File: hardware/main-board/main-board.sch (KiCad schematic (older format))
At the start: 76 parts, among them J1 USB_B_Micro, J2 STDC14, J3 Display Connector, J4 Conn_01x02, SW1 SW_Push, SW2 SW_Push, SW3 SW_Push, SW4 SW_Push, SW5 SW_Detect, U1 TSL2591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

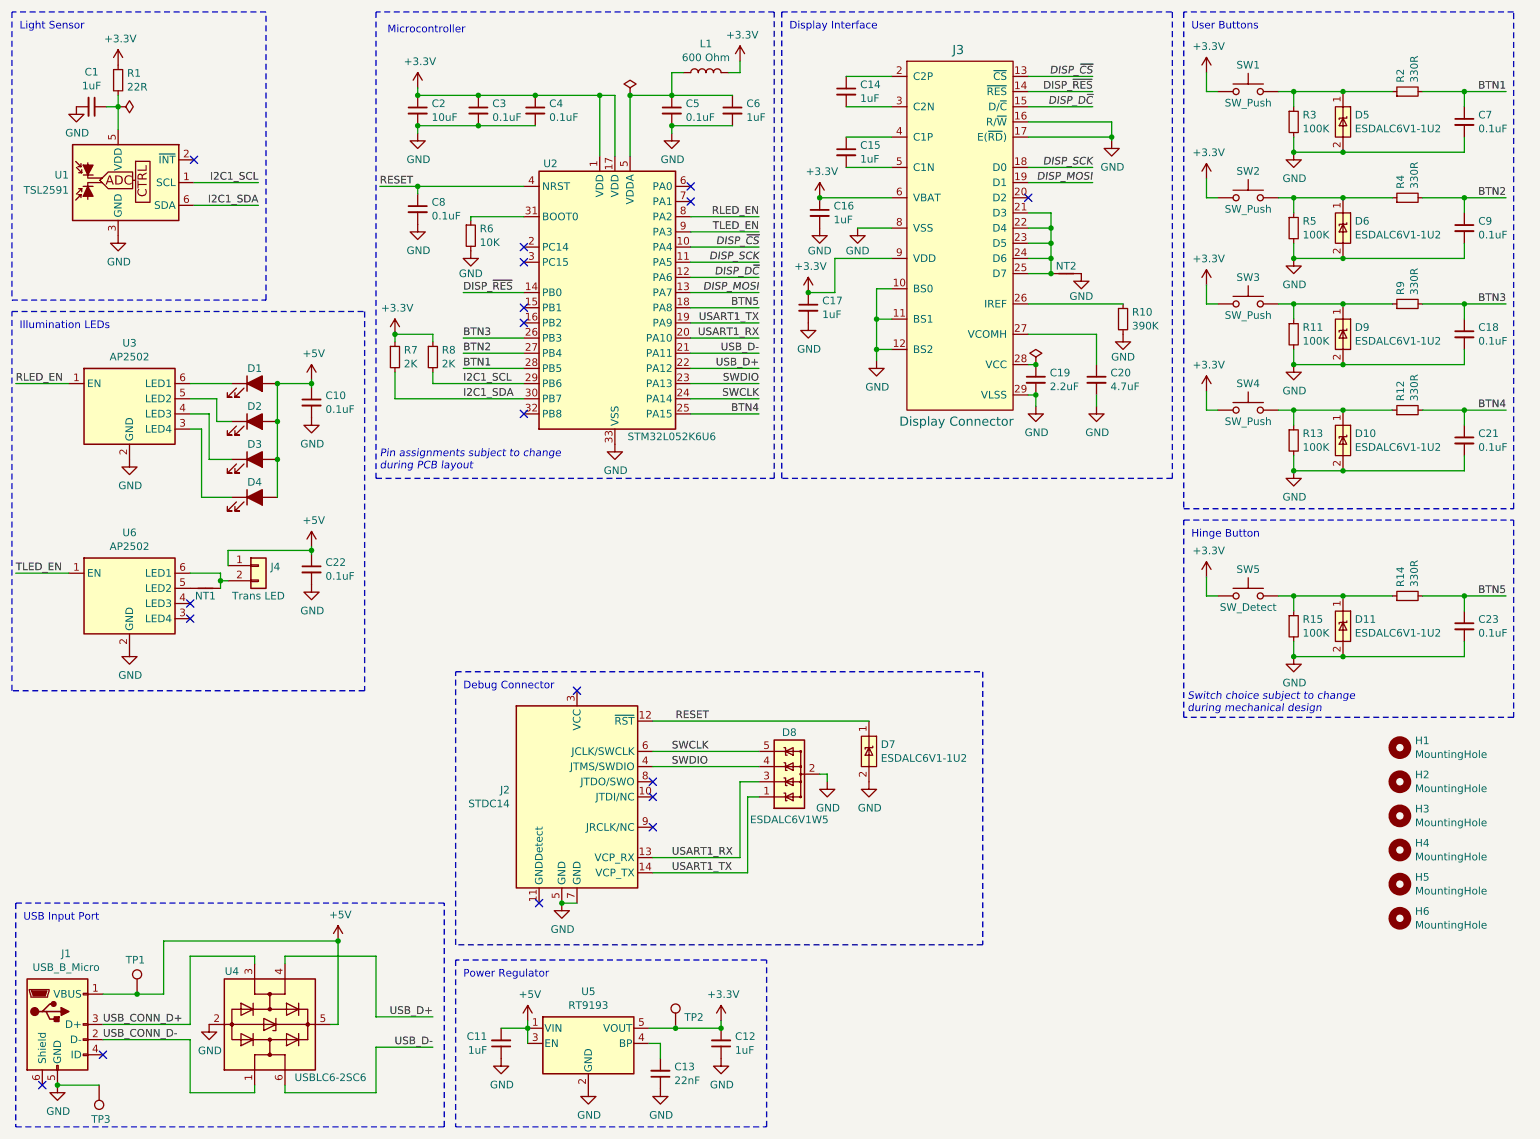
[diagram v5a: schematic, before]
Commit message: Power filtering changes
Added polyfuse and ferrite bead to Vbus power input.
Changed ferrite bead on VDDA to match the one used on the power input,
since they have similar specs and the other one was EOL.
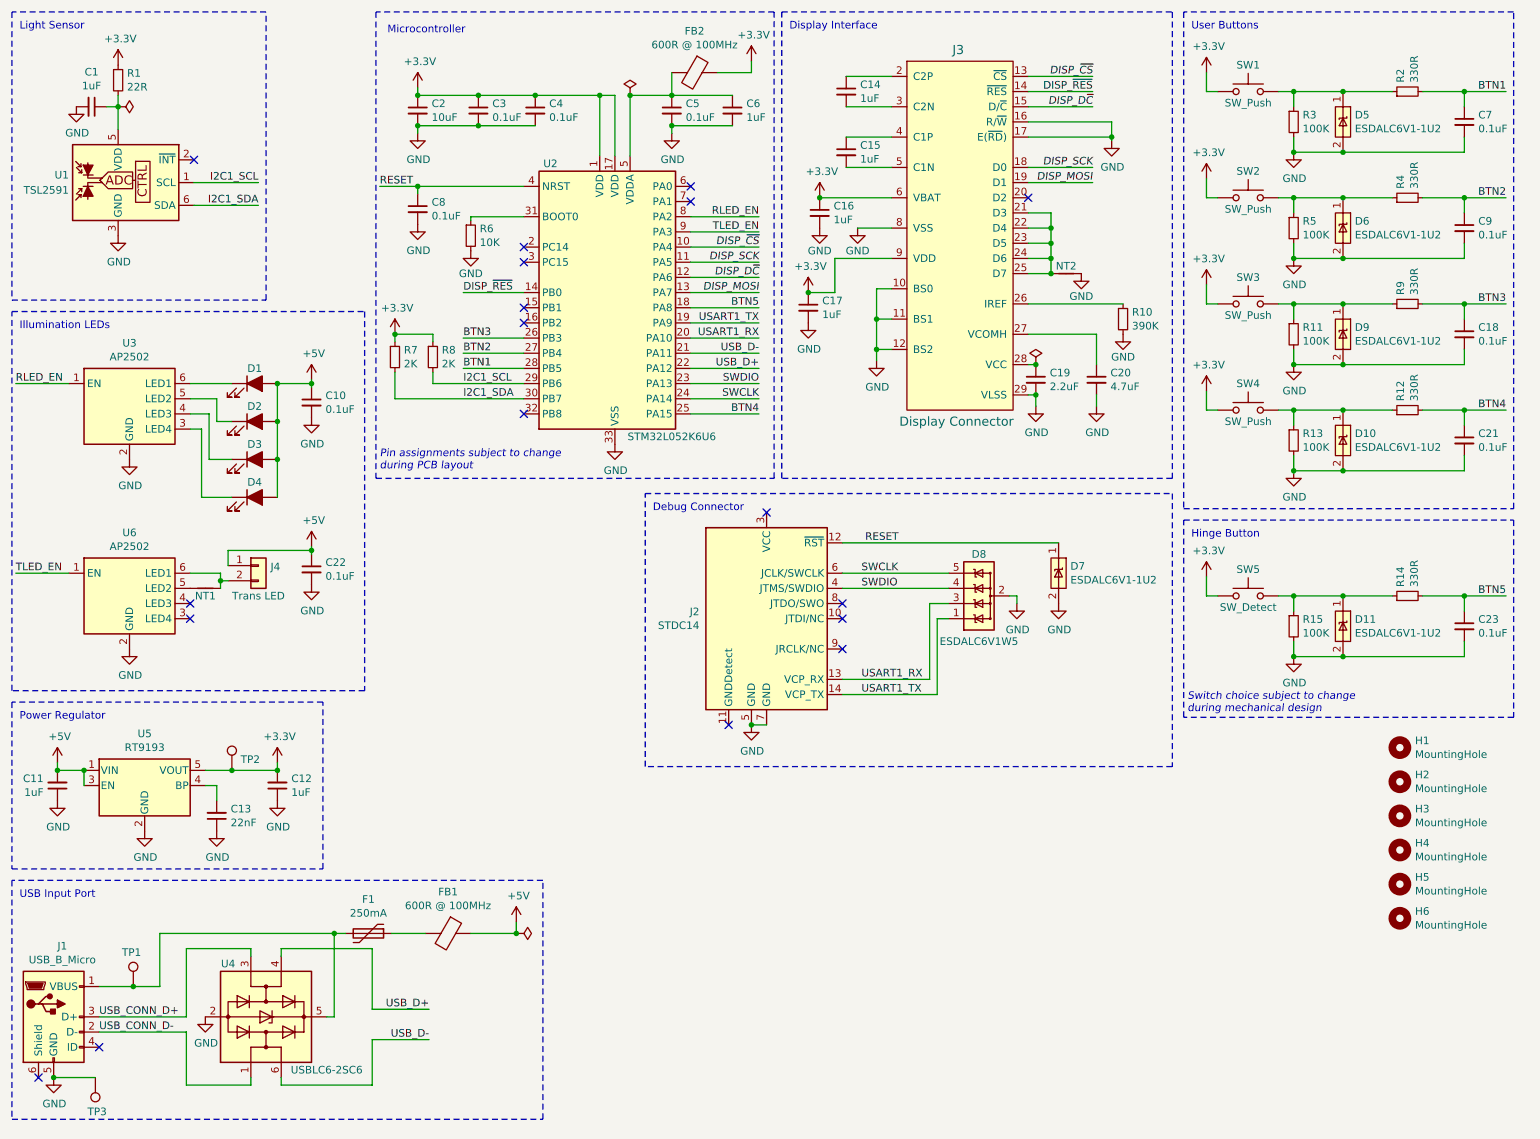
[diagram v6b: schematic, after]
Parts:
- removed L1: 600 Ohm, Inductor_SMD:L_0603_1608Metric, symbol Device:L
- added F1: 250mA, lib_fp:BF_0ZCJ_1206, symbol Device:Polyfuse
- added FB1, FB2: 600R @ 100MHz, Inductor_SMD:L_0603_1608Metric, symbol Device:Ferrite_Bead
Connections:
- net +3V3: now also FB2.1
- net +5V: now also FB1.1; no longer J1.1 (VBUS), TP1.1, U4.5 (VBUS)
- net at C5.1, C6.1, U2.5 (VDDA): now also FB2.2
- new net: F1.2, J1.1 (VBUS), TP1.1, U4.5 (VBUS)
- new net: F1.1, FB1.2
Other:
- moved on the sheet: C11, C12, C13, D7, D8, J1, J2, TP1, TP2, TP3, U4, U5

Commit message: Board layout work in progress
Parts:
- J4: footprint Connector_JST:JST_PH_B2B-PH-K_1x02_P2.00mm_Vertical -> Connector_JST:JST_SH_BM02B-SRSS-TB_1x02-1MP_P1.00mm_Vertical; Description CONN HEADER VERT 2POS 2MM -> CONN HEADER SMD 2POS 1MM; Manufacturer PN B2B-PH-K-S(LF)(SN) -> BM02B-SRSS-TB(LF)(SN); Supplier PN 455-1704-ND -> 455-1788-1-ND
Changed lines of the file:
@@
 F 0 "J4" H 2255 4192 50  0000 L CNN
 F 1 "Conn_01x02" H 1950 4000 50  0001 L CNN
-F 2 "Connector_JST:JST_PH_B2B-PH-K_1x02_P2.00mm_Vertical" H 2175 4200 50  0001 C CNN
+F 2 "Connector_JST:JST_SH_BM02B-SRSS-TB_1x02-1MP_P1.00mm_Vertical" H 2175 4200 50  0001 C CNN
 F 3 "http://www.jst-mfg.com/product/pdf/eng/ePH.pdf" H 2175 4200 50  0001 C CNN
 F 4 "Trans LED" H 2175 4000 50  0000 C CNN "User Label"
-F 5 "CONN HEADER VERT 2POS 2MM" H 2175 4200 50  0001 C CNN "Description"
+F 5 "CONN HEADER SMD 2POS 1MM" H 2175 4200 50  0001 C CNN "Description"
 F 6 "JST Sales America Inc." H 2175 4200 50  0001 C CNN "Manufacturer"
-F 7 "B2B-PH-K-S(LF)(SN)" H 2175 4200 50  0001 C CNN "Manufacturer PN"
+F 7 "BM02B-SRSS-TB(LF)(SN)" H 2175 4200 50  0001 C CNN "Manufacturer PN"
 F 8 "Digi-Key" H 2175 4200 50  0001 C CNN "Supplier"
-F 9 "455-1704-ND" H 2175 4200 50  0001 C CNN "Supplier PN"
+F 9 "455-1788-1-ND" H 2175 4200 50  0001 C CNN "Supplier PN"
 	1    2175 4200
 	1    0    0    -1

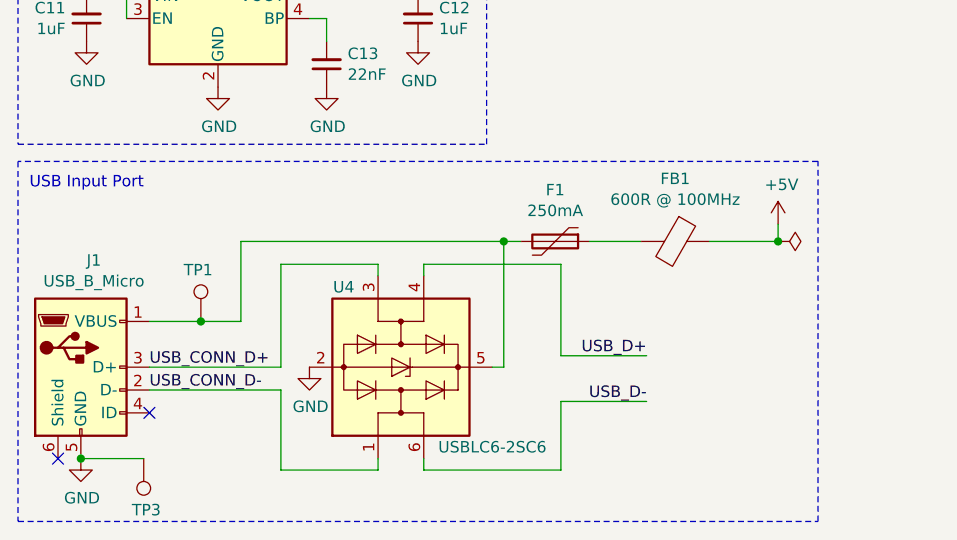
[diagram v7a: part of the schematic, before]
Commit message: More board layout work
Most components now placed, power and ground planes in place. Many areas
routed, but a lot of inter-section routing work is still TBD.
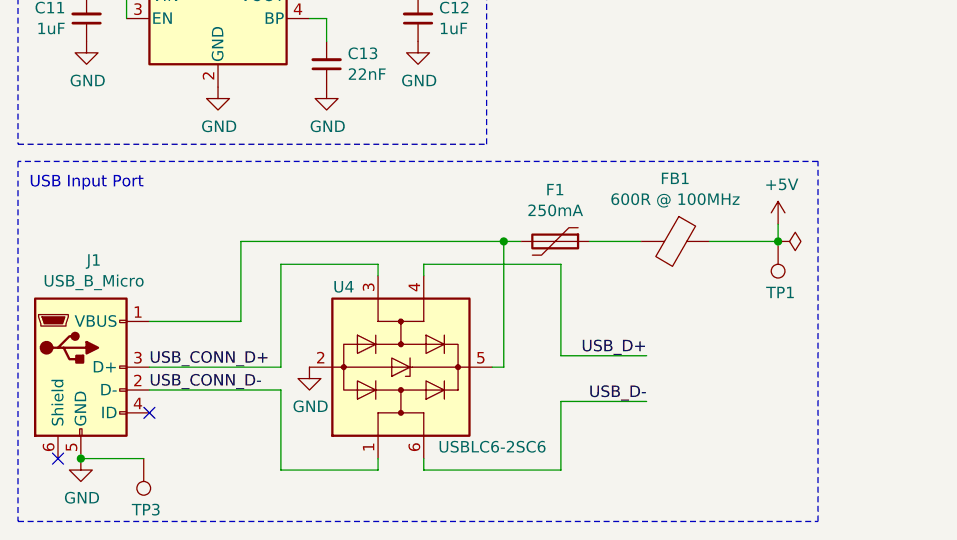
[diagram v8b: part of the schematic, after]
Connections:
- net +5V: now also TP1.1
- net at F1.2, J1.1 (VBUS), U4.5 (VBUS): no longer TP1.1
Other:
- moved on the sheet: TP1
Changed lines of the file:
@@
 L Connector:TestPoint TP1
 U 1 1 6066F1AB
-P 1350 6975
-F 0 "TP1" H 1275 7200 50  0000 L CNN
-F 1 "5V" H 1408 7002 50  0001 L CNN
-F 2 "TestPoint:TestPoint_Keystone_5005-5009_Compact" H 1550 6975 50  0001 C CNN
-F 3 "http://www.keyelco.com/product-pdf.cfm?p=1314" H 1550 6975 50  0001 C CNN
-F 4 "PC TEST POINT COMPACT BLACK" H 1350 6975 50  0001 C CNN "Description"
-F 5 "Keystone Electronics" H 1350 6975 50  0001 C CNN "Manufacturer"
-F 6 "5006" H 1350 6975 50  0001 C CNN "Manufacturer PN"
-F 7 "Digi-Key" H 1350 6975 50  0001 C CNN "Supplier"
-F 8 "36-5006-ND" H 1350 6975 50  0001 C CNN "Supplier PN"
-	1    1350 6975
-	1    0    0    -1
+P 3875 6625
+F 0 "TP1" H 3800 6850 50  0000 L CNN
+F 1 "5V" H 3933 6652 50  0001 L CNN
+F 2 "TestPoint:TestPoint_Keystone_5005-5009_Compact" H 4075 6625 50  0001 C CNN
+F 3 "http://www.keyelco.com/product-pdf.cfm?p=1314" H 4075 6625 50  0001 C CNN
+F 4 "PC TEST POINT COMPACT BLACK" H 3875 6625 50  0001 C CNN "Description"
+F 5 "Keystone Electronics" H 3875 6625 50  0001 C CNN "Manufacturer"
+F 6 "5006" H 3875 6625 50  0001 C CNN "Manufacturer PN"
+F 7 "Digi-Key" H 3875 6625 50  0001 C CNN "Supplier"
+F 8 "36-5006-ND" H 3875 6625 50  0001 C CNN "Supplier PN"
+	1    3875 6625
+	-1   0    0    1
 $EndComp
 NoConn ~ 725  7575
@@
 NoConn ~ 5025 1800
 NoConn ~ 1125 7375
-Connection ~ 1350 6975
-Wire Wire Line
-	1350 6975 1525 6975
 Wire Wire Line
 	1525 6975 1525 6625
@@
 	2675 7175 2625 7175
 Connection ~ 2675 6625
-Wire Wire Line
-	1125 6975 1350 6975
 $Comp
 L Device:C_Small C4
@@
 $EndComp
 Connection ~ 3875 6625
+Wire Wire Line
+	1125 6975 1525 6975
 $EndSCHEMATC
